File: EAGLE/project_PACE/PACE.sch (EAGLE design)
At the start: 25 parts, among them J3 PTH, U2 MPM3630GQV-P

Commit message: Replace micro usb with usb c
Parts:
- CAM1, CAM2, CAM3, CAM4: value 10118194-0001LF -> USB-C; device USB_Micro_B_v2:10118194-0001LF -> USB-C:USB-C
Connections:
- net 5VO: now also CAM1.A4/VBUS, CAM1.A9/VBUS, CAM2.A4/VBUS, CAM2.A9/VBUS, CAM3.A4/VBUS, CAM3.A9/VBUS, CAM4.A4/VBUS, CAM4.A9/VBUS; no longer CAM1.1, CAM2.1, CAM3.1, CAM4.1
- net GND: now also CAM1.B1/GND, CAM1.B12/GND, CAM2.B1/GND, CAM2.B12/GND, CAM3.B1/GND, CAM3.B12/GND, CAM4.B1/GND, CAM4.B12/GND; no longer CAM1.5, CAM2.5, CAM3.5, CAM4.5
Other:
- note added: "CAM PORTS"

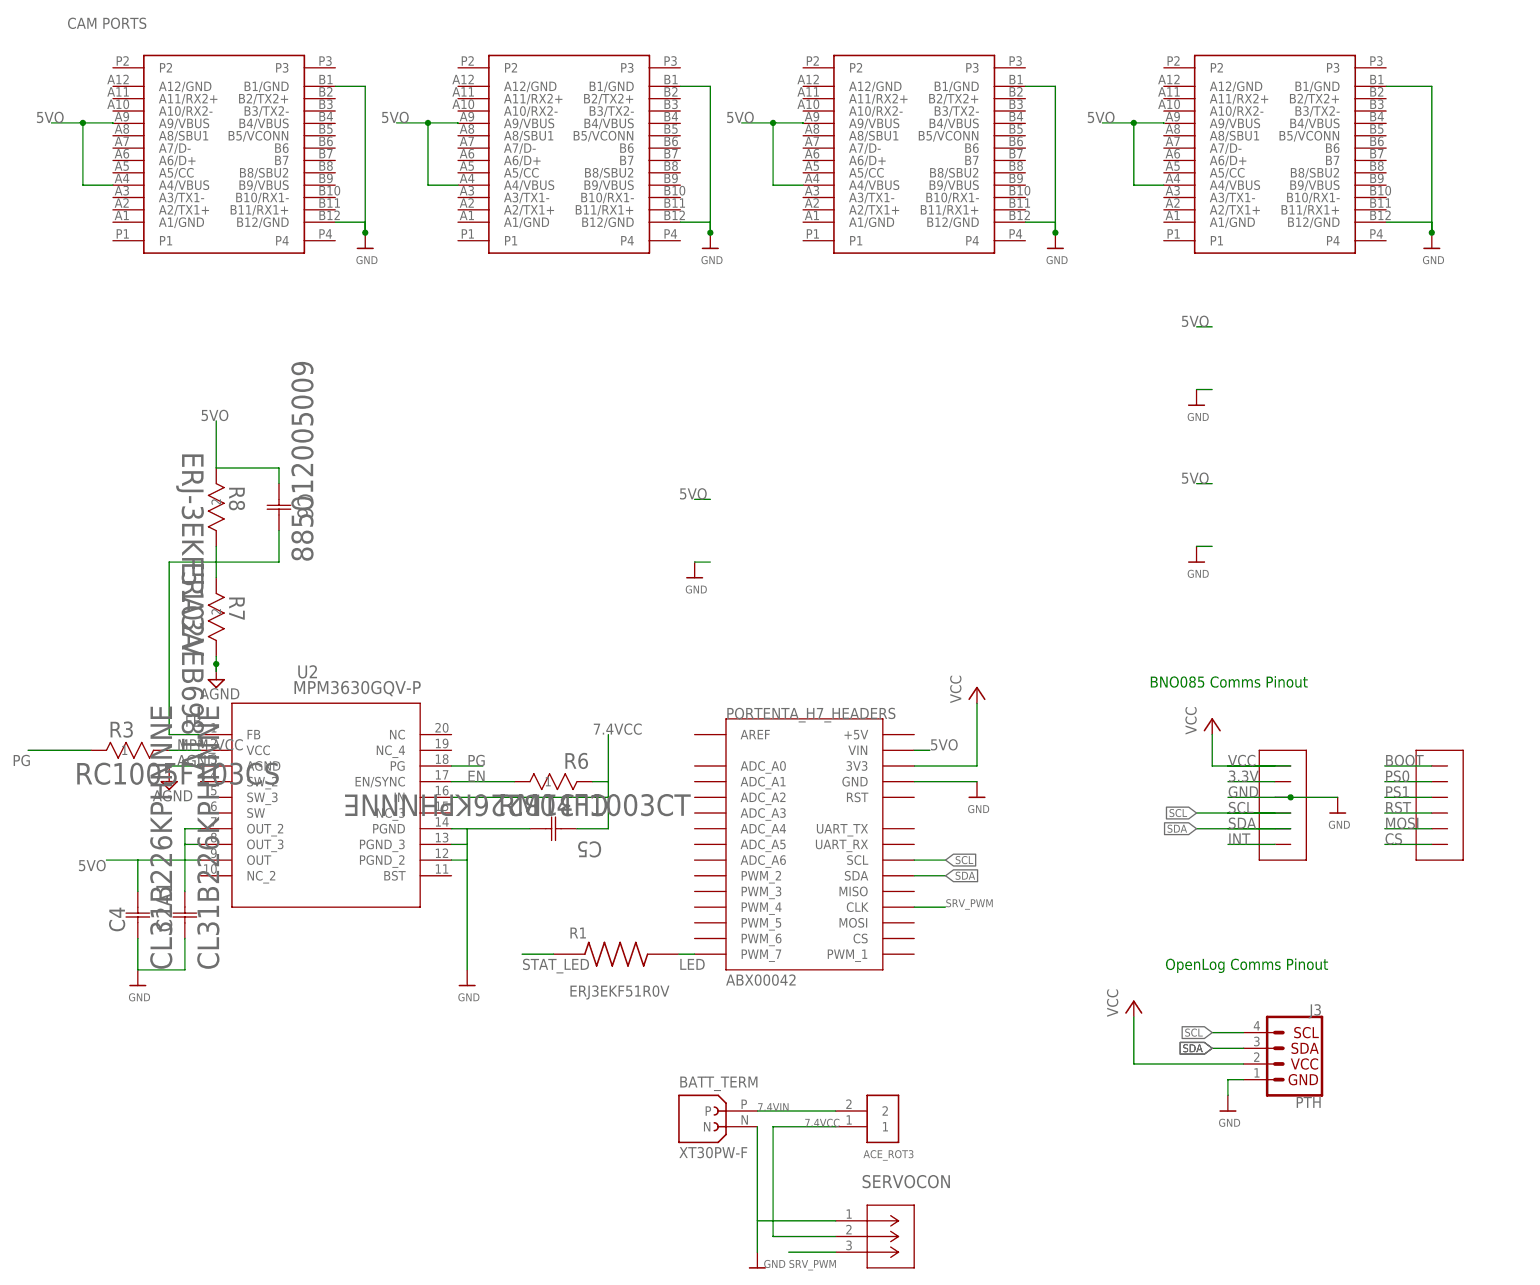
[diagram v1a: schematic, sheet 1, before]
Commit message: Update USB-C with Molex mfg part
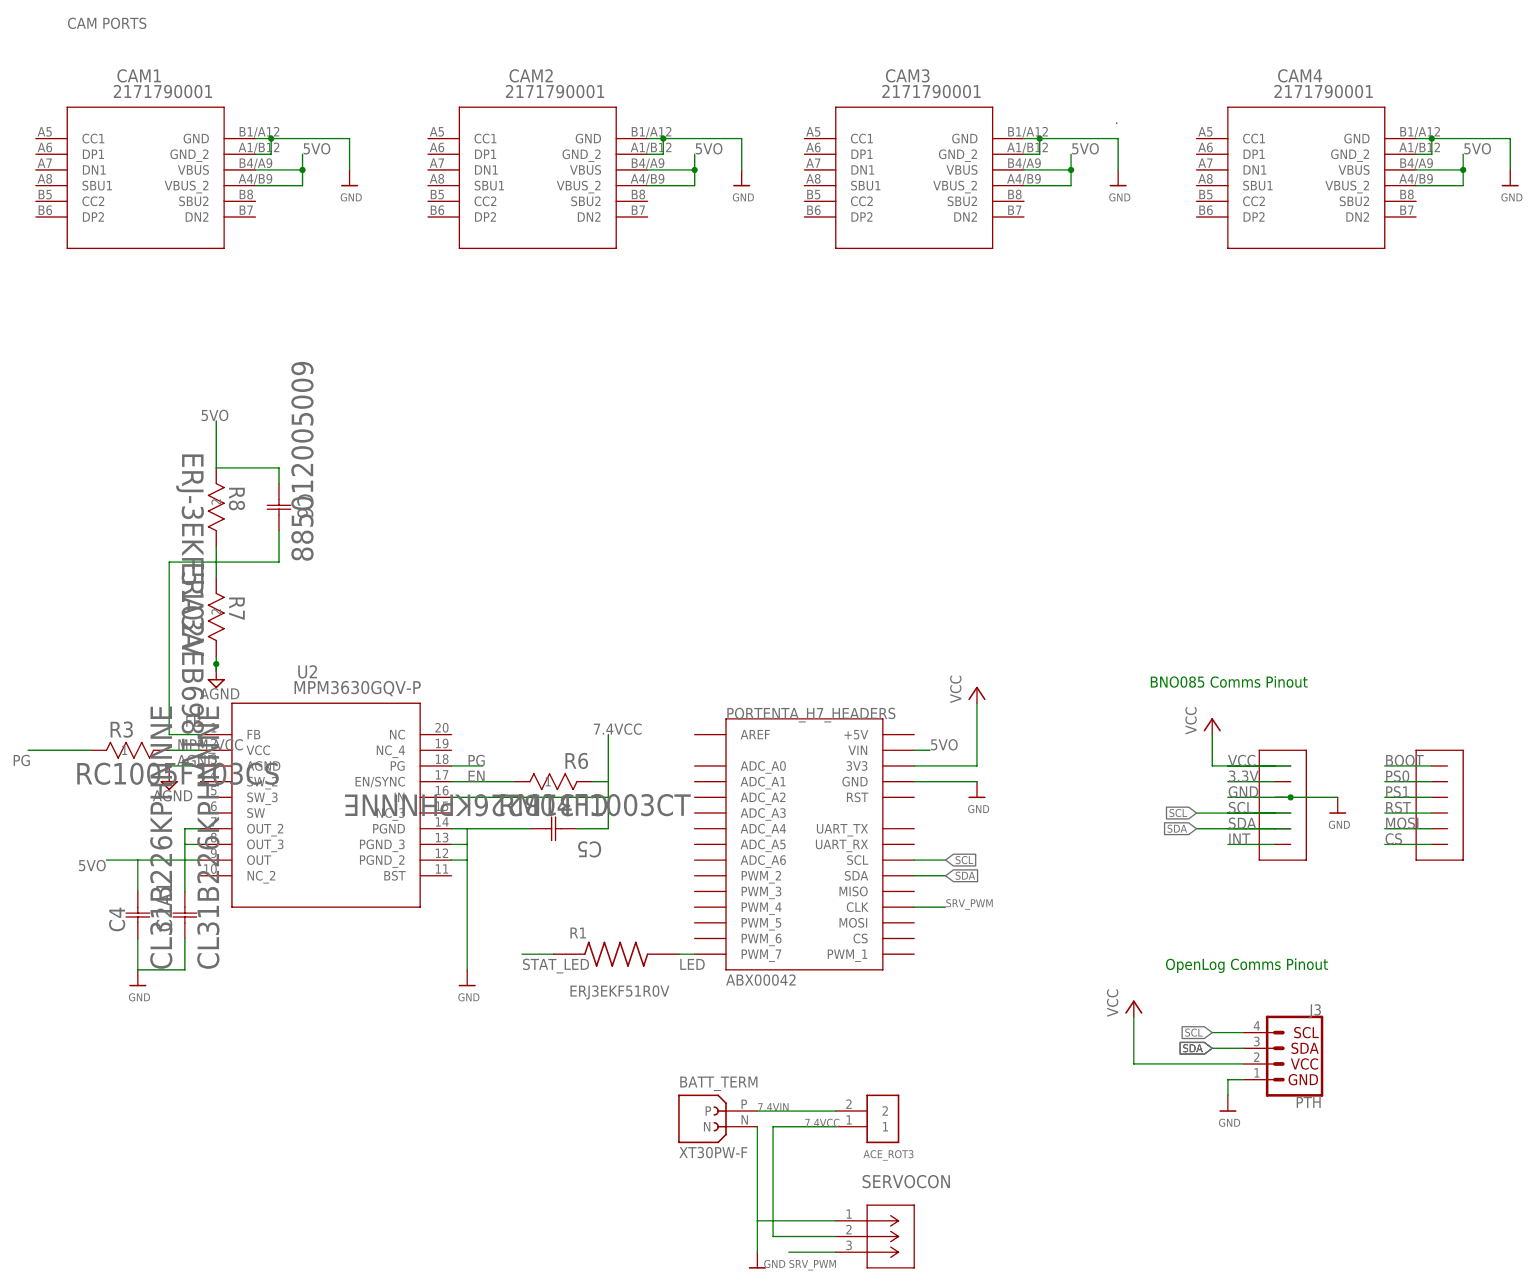
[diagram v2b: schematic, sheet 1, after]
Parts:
- removed U$1, U$3: MOUNTINGHOLE2.0, microbuilder:MOUNTINGHOLE2.0
- CAM1, CAM2, CAM3, CAM4: value USB-C -> 2171790001; device USB-C:USB-C -> MOLEX-2171790001-USB_C:2171790001
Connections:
- net 5VO: now also CAM1.VBUS, CAM1.VBUS_2, CAM2.VBUS, CAM2.VBUS_2, CAM3.VBUS, CAM3.VBUS_2, CAM4.VBUS, CAM4.VBUS_2; no longer CAM1.A4/VBUS, CAM1.A9/VBUS, CAM2.A4/VBUS, CAM2.A9/VBUS, CAM3.A4/VBUS, CAM3.A9/VBUS, CAM4.A4/VBUS, CAM4.A9/VBUS
- net GND: now also CAM1.GND, CAM1.GND_2, CAM2.GND, CAM2.GND_2, CAM3.GND, CAM3.GND_2, CAM4.GND, CAM4.GND_2; no longer CAM1.B1/GND, CAM1.B12/GND, CAM2.B1/GND, CAM2.B12/GND, CAM3.B1/GND, CAM3.B12/GND, CAM4.B1/GND, CAM4.B12/GND
